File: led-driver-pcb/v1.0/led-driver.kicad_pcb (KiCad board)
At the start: 2 copper layers, 39 x 48 mm, 44 parts, among them M3A P***, M3B P***, M3C P***, M3D P***, P1 POWER, P2 CTRL, P3 LED, Q1 MOSFET_N, Q2 MOSFET_N, U1 MAX16834

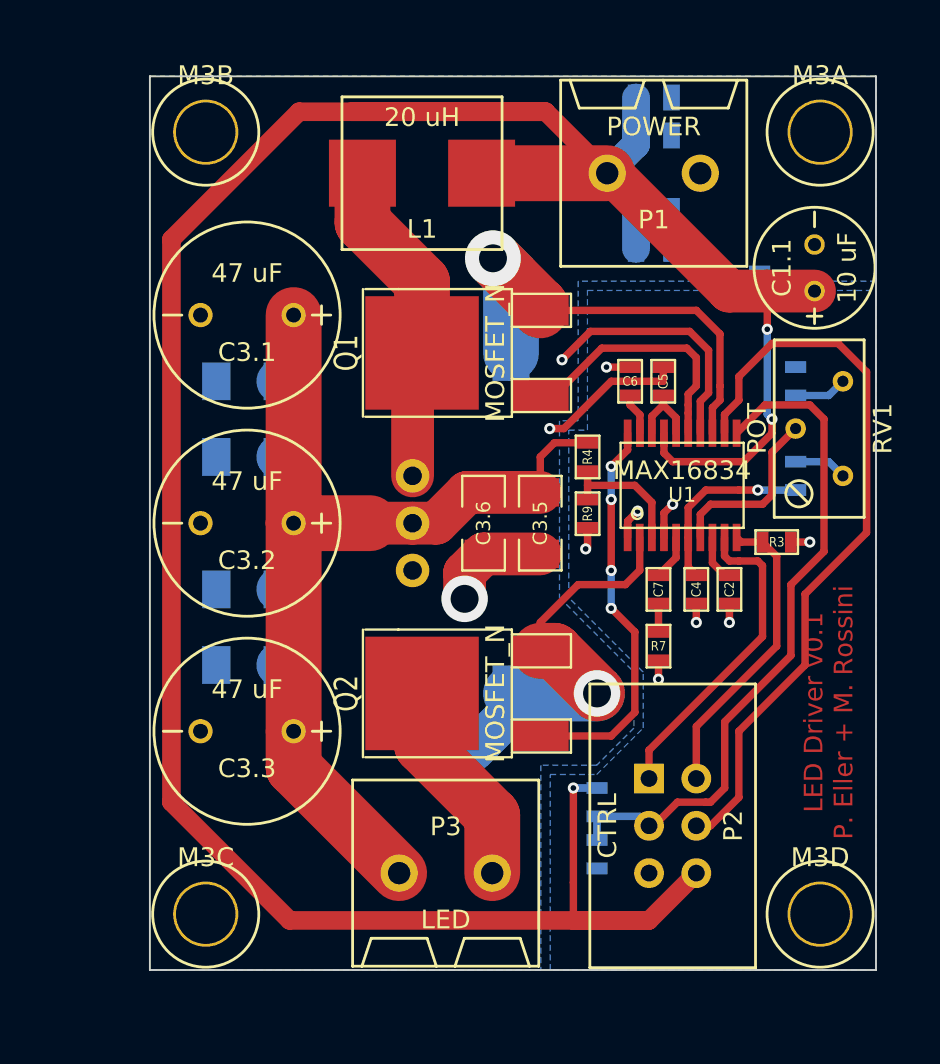
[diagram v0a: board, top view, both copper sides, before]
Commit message: Corrected the footprint of the MOSFETs.
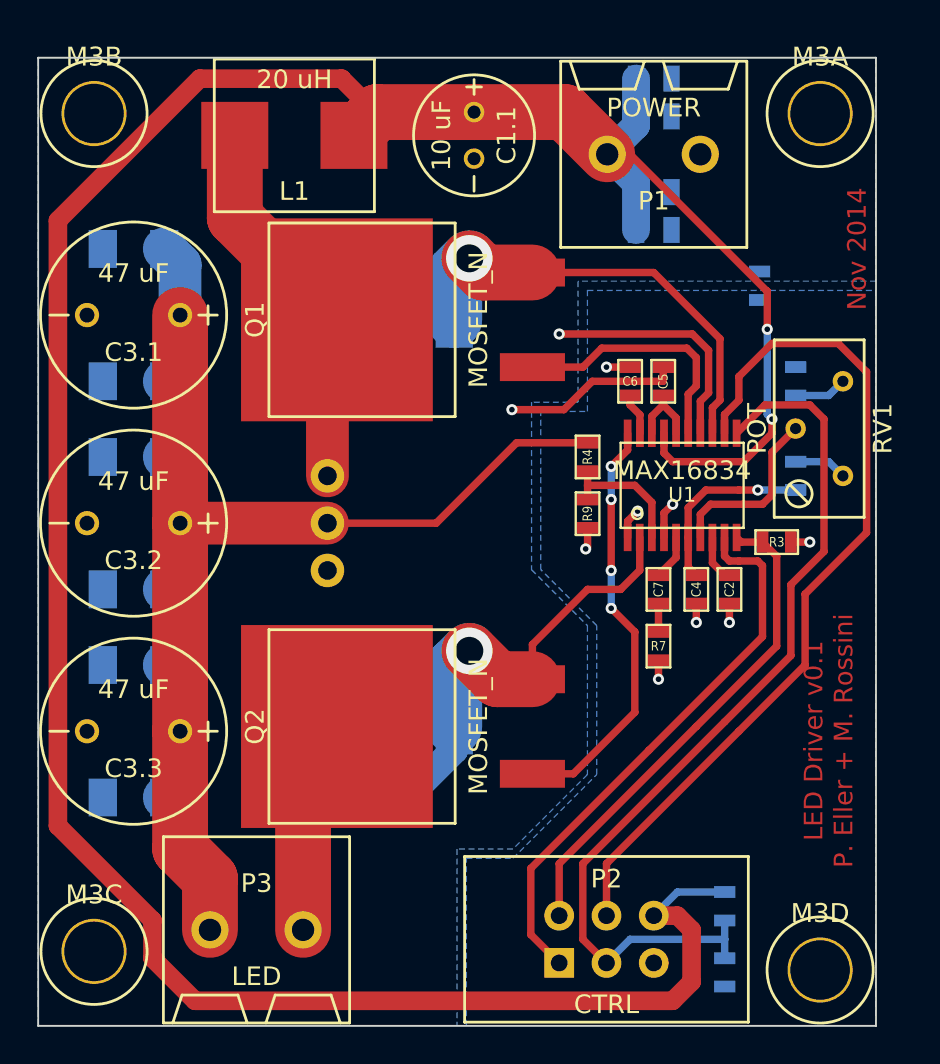
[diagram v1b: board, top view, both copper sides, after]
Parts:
- C3.5, C3.6: moved to B.Cu
- Q1, Q2: footprint DPAKGDS -> D2PAK
- moved C3.5 26.3 mm to (176.1, 164.7), turned to 0 degrees
- moved C3.6 23.9 mm to (176.1, 135.3), turned to 0 degrees
- moved C1.1 19.6 mm to (194.4, 129.2), turned to 270 degrees
- moved P3 10.6 mm to (182.7, 171.8)
- moved R2 9.35 mm to (207.9, 174.1)
- moved R1 8.85 mm to (207.9, 170.6)
- moved L1 7.15 mm to (184.8, 129.2)
- moved P2 7.06 mm to (201.5, 172.4), turned to 0 degrees
- moved M3C 6.32 mm to (174.0, 173.0)
- moved C3.1 6.10 mm to (176.1, 138.8)
- moved C3.2 6.10 mm to (176.1, 150.0)
- moved C3.3 6.10 mm to (176.1, 161.2)
- moved C3.4 6.10 mm to (176.1, 142.4)
- moved C3.7 6.10 mm to (176.1, 146.4)
- moved C3.8 6.10 mm to (176.1, 153.6)
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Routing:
- net N-000004: track 17.2 -> 30.4 mm
- net N-0000010: track 36.8 -> 49.6 mm
- net N-000005: track 16.3 -> 26.7 mm
- net N-0000024: track 70.5 -> 80.8 mm
- net N-000001: track 40.2 -> 46.6 mm
- net GNDPWR: track 27.4 -> 22.5 mm, vias 3 -> 2
- net N-0000021: track 162.9 -> 159.4 mm, vias 3 -> 2
- net N-0000019: track 17.8 -> 20.8 mm
- net N-0000020: track 22.3 -> 23.6 mm
- net N-0000014: track 21.5 -> 22.8 mm
- net N-0000013: track 25.0 -> 24.1 mm
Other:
- board size 39 x 48 mm -> 45 x 52 mm
- board text added: "Nov 2014"

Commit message: Moved two ceramic capacitors closer to the diode.
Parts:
- C3.5, C3.6: moved to F.Cu
- moved C3.5 20.2 mm to (191.9, 152.0), turned to 180 degrees
- moved C3.6 20.2 mm to (191.9, 148.0), turned to 180 degrees
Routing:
- net GNDPWR: track 22.5 -> 29.0 mm, vias 2 -> 3
- net N-0000024: track 80.8 -> 77.0 mm
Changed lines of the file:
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@@
     (thickness 1.6)
     (drawings 8)
-    (tracks 220)
+    (tracks 227)
     (zones 0)
     (modules 44)
@@
   )
   (setup
-    (last_trace_width 0.4)
+    (last_trace_width 2.3)
     (user_trace_width 1)
     (user_trace_width 1.5)
@@
     )
   )
-  (module SM1206 (layer B.Cu)
-    (at 176.124 135.268)
-    (attr smd)
-    (fp_text reference C3.6 (at 0 0) (layer B.SilkS)
-      (effects (font (size 0.762 0.762) (thickness 0.127)) (justify mirror))
-    )
-    (fp_text value "1 uF" (at 0 0) (layer B.SilkS) hide
-      (effects (font (size 0.762 0.762) (thickness 0.127)) (justify mirror))
-    )
-    (fp_line (start -2.54 1.143) (end -2.54 -1.143) (layer B.SilkS) (width 0.127))
-    (fp_line (start -2.54 -1.143) (end -0.889 -1.143) (layer B.SilkS) (width 0.127))
-    (fp_line (start 0.889 1.143) (end 2.54 1.143) (layer B.SilkS) (width 0.127))
-    (fp_line (start 2.54 1.143) (end 2.54 -1.143) (layer B.SilkS) (width 0.127))
-    (fp_line (start 2.54 -1.143) (end 0.889 -1.143) (layer B.SilkS) (width 0.127))
-    (fp_line (start -0.889 1.143) (end -2.54 1.143) (layer B.SilkS) (width 0.127))
-    (pad 1 smd rect (at -1.651 0) (size 1.524 2.032)
-      (layers B.Cu B.Mask)
-      (net 2 GNDPWR)
-    )
-    (pad 2 smd rect (at 1.651 0) (size 1.524 2.032)
-      (layers B.Cu B.Mask)
+  (module SM1206 (layer F.Cu)
+    (at 191.872 147.968 180)
+    (attr smd)
+    (fp_text reference C3.6 (at 0 0 180) (layer F.SilkS)
+      (effects (font (size 0.762 0.762) (thickness 0.127)))
+    )
+    (fp_text value "1 uF" (at 0 0 180) (layer F.SilkS) hide
+      (effects (font (size 0.762 0.762) (thickness 0.127)))
+    )
+    (fp_line (start -2.54 -1.143) (end -2.54 1.143) (layer F.SilkS) (width 0.127))
+    (fp_line (start -2.54 1.143) (end -0.889 1.143) (layer F.SilkS) (width 0.127))
+    (fp_line (start 0.889 -1.143) (end 2.54 -1.143) (layer F.SilkS) (width 0.127))
+    (fp_line (start 2.54 -1.143) (end 2.54 1.143) (layer F.SilkS) (width 0.127))
+    (fp_line (start 2.54 1.143) (end 0.889 1.143) (layer F.SilkS) (width 0.127))
+    (fp_line (start -0.889 -1.143) (end -2.54 -1.143) (layer F.SilkS) (width 0.127))
+    (pad 1 smd rect (at -1.651 0 180) (size 1.524 2.032)
+      (layers F.Cu F.Mask)
+      (net 2 GNDPWR)
+    )
+    (pad 2 smd rect (at 1.651 0 180) (size 1.524 2.032)
+      (layers F.Cu F.Mask)
       (net 17 N-0000024)
     )
@@
     )
   )
-  (module SM1206 (layer B.Cu)
-    (at 176.124 164.732)
-    (attr smd)
-    (fp_text reference C3.5 (at 0 0) (layer B.SilkS)
-      (effects (font (size 0.762 0.762) (thickness 0.127)) (justify mirror))
-    )
-    (fp_text value "1 uF" (at 0 0) (layer B.SilkS) hide
-      (effects (font (size 0.762 0.762) (thickness 0.127)) (justify mirror))
-    )
-    (fp_line (start -2.54 1.143) (end -2.54 -1.143) (layer B.SilkS) (width 0.127))
-    (fp_line (start -2.54 -1.143) (end -0.889 -1.143) (layer B.SilkS) (width 0.127))
-    (fp_line (start 0.889 1.143) (end 2.54 1.143) (layer B.SilkS) (width 0.127))
-    (fp_line (start 2.54 1.143) (end 2.54 -1.143) (layer B.SilkS) (width 0.127))
-    (fp_line (start 2.54 -1.143) (end 0.889 -1.143) (layer B.SilkS) (width 0.127))
-    (fp_line (start -0.889 1.143) (end -2.54 1.143) (layer B.SilkS) (width 0.127))
-    (pad 1 smd rect (at -1.651 0) (size 1.524 2.032)
-      (layers B.Cu B.Mask)
-      (net 2 GNDPWR)
-    )
-    (pad 2 smd rect (at 1.651 0) (size 1.524 2.032)
-      (layers B.Cu B.Mask)
+  (module SM1206 (layer F.Cu)
+    (at 191.872 152.032 180)
+    (attr smd)
+    (fp_text reference C3.5 (at 0 0 180) (layer F.SilkS)
+      (effects (font (size 0.762 0.762) (thickness 0.127)))
+    )
+    (fp_text value "1 uF" (at 0 0 180) (layer F.SilkS) hide
+      (effects (font (size 0.762 0.762) (thickness 0.127)))
+    )
+    (fp_line (start -2.54 -1.143) (end -2.54 1.143) (layer F.SilkS) (width 0.127))
+    (fp_line (start -2.54 1.143) (end -0.889 1.143) (layer F.SilkS) (width 0.127))
+    (fp_line (start 0.889 -1.143) (end 2.54 -1.143) (layer F.SilkS) (width 0.127))
+    (fp_line (start 2.54 -1.143) (end 2.54 1.143) (layer F.SilkS) (width 0.127))
+    (fp_line (start 2.54 1.143) (end 0.889 1.143) (layer F.SilkS) (width 0.127))
+    (fp_line (start -0.889 -1.143) (end -2.54 -1.143) (layer F.SilkS) (width 0.127))
+    (pad 1 smd rect (at -1.651 0 180) (size 1.524 2.032)
+      (layers F.Cu F.Mask)
+      (net 2 GNDPWR)
+    )
+    (pad 2 smd rect (at 1.651 0 180) (size 1.524 2.032)
+      (layers F.Cu F.Mask)
       (net 17 N-0000024)
     )
@@
   (segment (start 211.43 151.016) (end 212.446 151.016) (width 0.4) (layer F.Cu) (net 1))
   (via (at 212.446 151.016) (size 0.6) (layers F.Cu B.Cu) (net 1))
+  (segment (start 193.523 152.032) (end 193.523 150.127) (width 2.3) (layer F.Cu) (net 2))
+  (segment (start 193.523 150.127) (end 193.65 150) (width 2.3) (layer F.Cu) (net 2))
+  (segment (start 193.523 147.968) (end 193.523 149.873) (width 2.3) (layer F.Cu) (net 2))
+  (via (at 195.936 150) (size 2.5) (drill 1.5) (layers F.Cu B.Cu) (net 2))
+  (segment (start 193.65 150) (end 195.936 150) (width 2.3) (layer F.Cu) (net 2))
+  (segment (start 193.523 149.873) (end 193.65 150) (width 2.3) (layer F.Cu) (net 2))
   (segment (start 204.572 142.38) (end 200.762 142.38) (width 0.4) (layer F.Cu) (net 2))
   (segment (start 200.762 142.38) (end 199.238 143.904) (width 0.4) (layer F.Cu) (net 2))
@@
   (segment (start 204.572 143.65) (end 204.572 143.142) (width 0.4) (layer F.Cu) (net 16))
   (segment (start 205.26288 144.34088) (end 204.572 143.65) (width 0.4) (layer F.Cu) (net 16))
+  (segment (start 190.221 152.032) (end 190.221 150.127) (width 2.3) (layer F.Cu) (net 17))
+  (segment (start 190.221 150.127) (end 190.094 150) (width 2.3) (layer F.Cu) (net 17))
+  (segment (start 186.538 150) (end 190.094 150) (width 2.3) (layer F.Cu) (net 17))
+  (segment (start 190.221 149.873) (end 190.221 147.968) (width 2.3) (layer F.Cu) (net 17))
+  (segment (start 190.094 150) (end 190.221 149.873) (width 2.3) (layer F.Cu) (net 17))
+  (segment (start 200.508 145.682) (end 191.11 145.682) (width 0.4) (layer F.Cu) (net 17))
+  (segment (start 191.11 145.682) (end 190.221 146.571) (width 0.4) (layer F.Cu) (net 17))
+  (segment (start 190.221 146.571) (end 190.221 147.968) (width 0.4) (layer F.Cu) (net 17))
   (segment (start 178.624 161.176) (end 178.624 167.486) (width 3) (layer F.Cu) (net 17))
   (segment (start 180.228 169.09) (end 180.228 171.844) (width 3) (layer F.Cu) (net 17))
@@
   (segment (start 178.624 150) (end 178.624 161.176) (width 3) (layer F.Cu) (net 17))
   (segment (start 178.624 138.824) (end 178.624 150) (width 3) (layer F.Cu) (net 17))
-  (segment (start 200.508 145.682) (end 196.698 145.682) (width 0.4) (layer F.Cu) (net 17))
-  (segment (start 192.38 150) (end 186.538 150) (width 0.4) (layer F.Cu) (net 17))
-  (segment (start 196.698 145.682) (end 192.38 150) (width 0.4) (layer F.Cu) (net 17))
   (segment (start 186.538 150) (end 178.624 150) (width 2.3) (layer F.Cu) (net 17))
-  (segment (start 177.775 135.268) (end 178.624 136.117) (width 2.3) (layer B.Cu) (net 17))
-  (segment (start 178.624 136.117) (end 178.624 138.824) (width 2.3) (layer B.Cu) (net 17))
-  (segment (start 177.775 164.732) (end 178.624 163.883) (width 2.3) (layer B.Cu) (net 17))
-  (segment (start 178.624 163.883) (end 178.624 161.176) (width 2.3) (layer B.Cu) (net 17))
   (segment (start 177.775 157.62) (end 178.624 158.469) (width 2.3) (layer B.Cu) (net 17))
   (segment (start 178.624 158.469) (end 178.624 161.176) (width 2.3) (layer B.Cu) (net 17))
